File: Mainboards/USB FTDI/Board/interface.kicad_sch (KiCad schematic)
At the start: 16 parts, among them IC7 ADuM142E0BRQZ-RL7, IC8 ADuM142E0BRQZ-RL7, IC9 ADuM142E0BRQZ-RL7, X2 AKL18X-04W, X4 ALLSERIALMASTERM

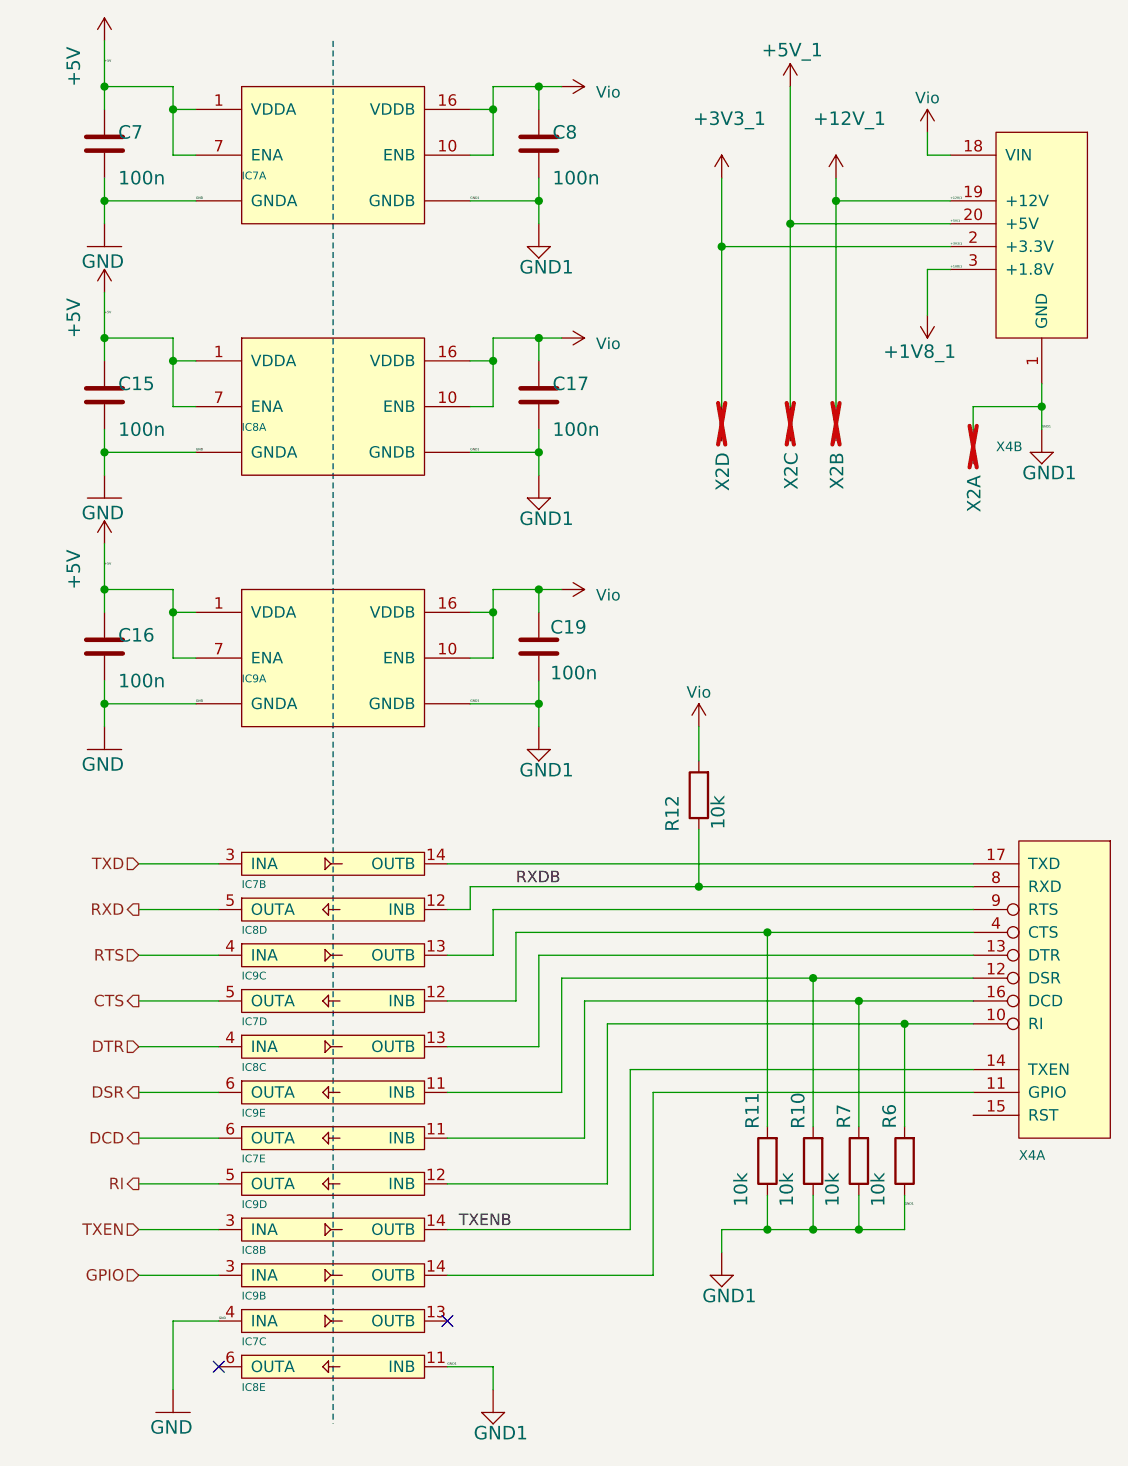
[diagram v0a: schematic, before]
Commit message: Remove pads from cutouts
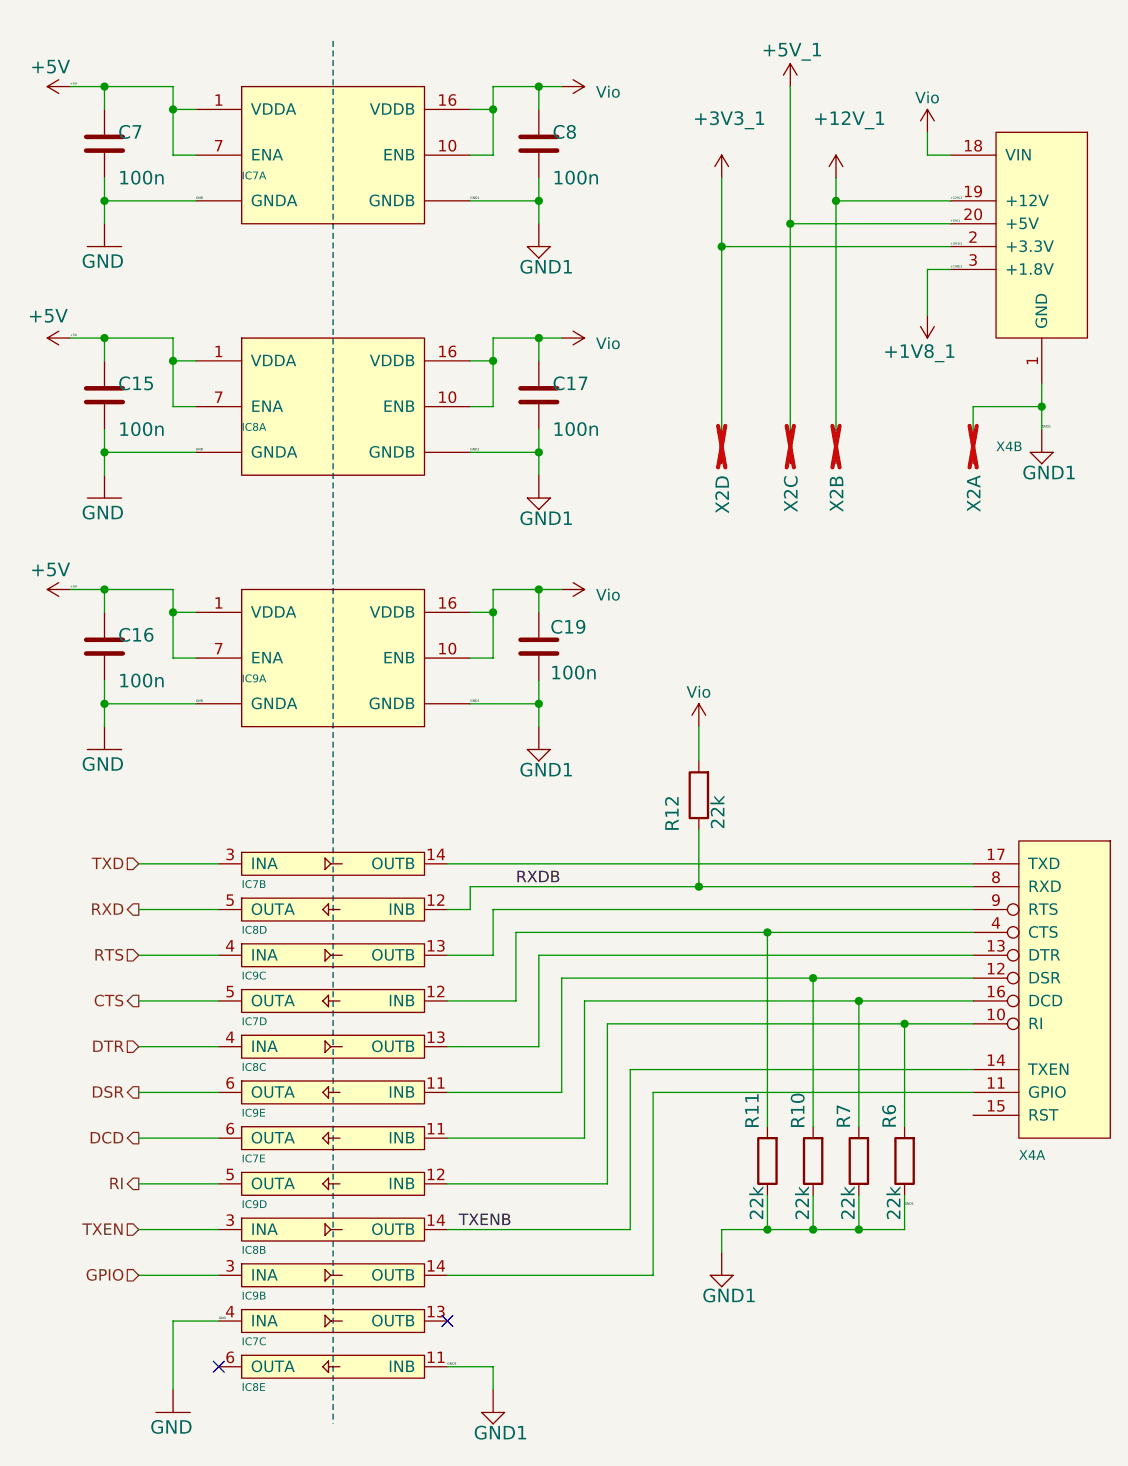
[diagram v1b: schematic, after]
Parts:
- R10, R11, R12, R6, R7: value 10k -> 22k; LCSC C17414 -> (none)
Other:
- moved on the sheet: X2B, X2C, X2D

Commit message: FTDI master: Change footprint of isolators
minor improvments
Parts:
- IC7, IC8, IC9: footprint Package_SO:SOIC-16_3.9x9.9mm_P1.27mm -> Package_SO:QSOP-16_3.9x4.9mm_P0.635mm; LCSC C208656 -> C660448
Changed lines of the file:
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@@
 			)
 		)
-		(property "Footprint" "Package_SO:SOIC-16_3.9x9.9mm_P1.27mm"
+		(property "Footprint" "Package_SO:QSOP-16_3.9x4.9mm_P0.635mm"
 			(at 92.71 128.27 0)
 			(effects
@@
 			)
 		)
-		(property "LCSC" "C208656"
+		(property "LCSC" "C660448"
 			(at 92.71 128.27 0)
 			(effects
@@
 			)
 		)
-		(property "Footprint" "Package_SO:SOIC-16_3.9x9.9mm_P1.27mm"
+		(property "Footprint" "Package_SO:QSOP-16_3.9x4.9mm_P0.635mm"
 			(at 92.71 143.51 0)
 			(effects
@@
 			)
 		)
-		(property "LCSC" "C208656"
+		(property "LCSC" "C660448"
 			(at 92.71 143.51 0)
 			(effects
@@
 			)
 		)
-		(property "Footprint" "Package_SO:SOIC-16_3.9x9.9mm_P1.27mm"
+		(property "Footprint" "Package_SO:QSOP-16_3.9x4.9mm_P0.635mm"
 			(at 92.71 113.03 0)
 			(effects
@@
 			)
 		)
-		(property "LCSC" "C208656"
+		(property "LCSC" "C660448"
 			(at 92.71 113.03 0)
 			(effects
@@
 			)
 		)
-		(property "Footprint" "Package_SO:SOIC-16_3.9x9.9mm_P1.27mm"
+		(property "Footprint" "Package_SO:QSOP-16_3.9x4.9mm_P0.635mm"
 			(at 92.71 163.83 0)
 			(effects
@@
 			)
 		)
-		(property "LCSC" "C208656"
+		(property "LCSC" "C660448"
 			(at 92.71 163.83 0)
 			(effects
@@
 			)
 		)
-		(property "Footprint" "Package_SO:SOIC-16_3.9x9.9mm_P1.27mm"
+		(property "Footprint" "Package_SO:QSOP-16_3.9x4.9mm_P0.635mm"
 			(at 92.71 34.29 0)
 			(effects
@@
 			)
 		)
-		(property "LCSC" "C208656"
+		(property "LCSC" "C660448"
 			(at 92.71 34.29 0)
 			(effects
@@
 			)
 		)
-		(property "Footprint" "Package_SO:SOIC-16_3.9x9.9mm_P1.27mm"
+		(property "Footprint" "Package_SO:QSOP-16_3.9x4.9mm_P0.635mm"
 			(at 92.71 158.75 0)
 			(effects
@@
 			)
 		)
-		(property "LCSC" "C208656"
+		(property "LCSC" "C660448"
 			(at 92.71 158.75 0)
 			(effects
@@
 			)
 		)
-		(property "Footprint" "Package_SO:SOIC-16_3.9x9.9mm_P1.27mm"
+		(property "Footprint" "Package_SO:QSOP-16_3.9x4.9mm_P0.635mm"
 			(at 92.71 123.19 0)
 			(effects
@@
 			)
 		)
-		(property "LCSC" "C208656"
+		(property "LCSC" "C660448"
 			(at 92.71 123.19 0)
 			(effects
@@
 			)
 		)
-		(property "Footprint" "Package_SO:SOIC-16_3.9x9.9mm_P1.27mm"
+		(property "Footprint" "Package_SO:QSOP-16_3.9x4.9mm_P0.635mm"
 			(at 92.71 90.17 0)
 			(effects
@@
 			)
 		)
-		(property "LCSC" "C208656"
+		(property "LCSC" "C660448"
 			(at 92.71 90.17 0)
 			(effects
@@
 			)
 		)
-		(property "Footprint" "Package_SO:SOIC-16_3.9x9.9mm_P1.27mm"
+		(property "Footprint" "Package_SO:QSOP-16_3.9x4.9mm_P0.635mm"
 			(at 92.71 148.59 0)
 			(effects
@@
 			)
 		)
-		(property "LCSC" "C208656"
+		(property "LCSC" "C660448"
 			(at 92.71 148.59 0)
 			(effects
@@
 			)
 		)
-		(property "Footprint" "Package_SO:SOIC-16_3.9x9.9mm_P1.27mm"
+		(property "Footprint" "Package_SO:QSOP-16_3.9x4.9mm_P0.635mm"
 			(at 92.71 138.43 0)
 			(effects
@@
 			)
 		)
-		(property "LCSC" "C208656"
+		(property "LCSC" "C660448"
 			(at 92.71 138.43 0)
 			(effects
@@
 			)
 		)
-		(property "Footprint" "Package_SO:SOIC-16_3.9x9.9mm_P1.27mm"
+		(property "Footprint" "Package_SO:QSOP-16_3.9x4.9mm_P0.635mm"
 			(at 92.71 168.91 0)
 			(effects
@@
 			)
 		)
-		(property "LCSC" "C208656"
+		(property "LCSC" "C660448"
 			(at 92.71 168.91 0)
 			(effects
@@
 			)
 		)
-		(property "Footprint" "Package_SO:SOIC-16_3.9x9.9mm_P1.27mm"
+		(property "Footprint" "Package_SO:QSOP-16_3.9x4.9mm_P0.635mm"
 			(at 92.71 118.11 0)
 			(effects
@@
 			)
 		)
-		(property "LCSC" "C208656"
+		(property "LCSC" "C660448"
 			(at 92.71 118.11 0)
 			(effects
@@
 			)
 		)
-		(property "Footprint" "Package_SO:SOIC-16_3.9x9.9mm_P1.27mm"
+		(property "Footprint" "Package_SO:QSOP-16_3.9x4.9mm_P0.635mm"
 			(at 92.71 133.35 0)
 			(effects
@@
 			)
 		)
-		(property "LCSC" "C208656"
+		(property "LCSC" "C660448"
 			(at 92.71 133.35 0)
 			(effects
@@
 			)
 		)
-		(property "Footprint" "Package_SO:SOIC-16_3.9x9.9mm_P1.27mm"
+		(property "Footprint" "Package_SO:QSOP-16_3.9x4.9mm_P0.635mm"
 			(at 92.71 153.67 0)
 			(effects
@@
 			)
 		)
-		(property "LCSC" "C208656"
+		(property "LCSC" "C660448"
 			(at 92.71 153.67 0)
 			(effects
@@
 			)
 		)
-		(property "Footprint" "Package_SO:SOIC-16_3.9x9.9mm_P1.27mm"
+		(property "Footprint" "Package_SO:QSOP-16_3.9x4.9mm_P0.635mm"
 			(at 92.71 62.23 0)
 			(effects
@@
 			)
 		)
-		(property "LCSC" "C208656"
+		(property "LCSC" "C660448"
 			(at 92.71 62.23 0)
 			(effects
